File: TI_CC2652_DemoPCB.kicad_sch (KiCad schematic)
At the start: 4 parts

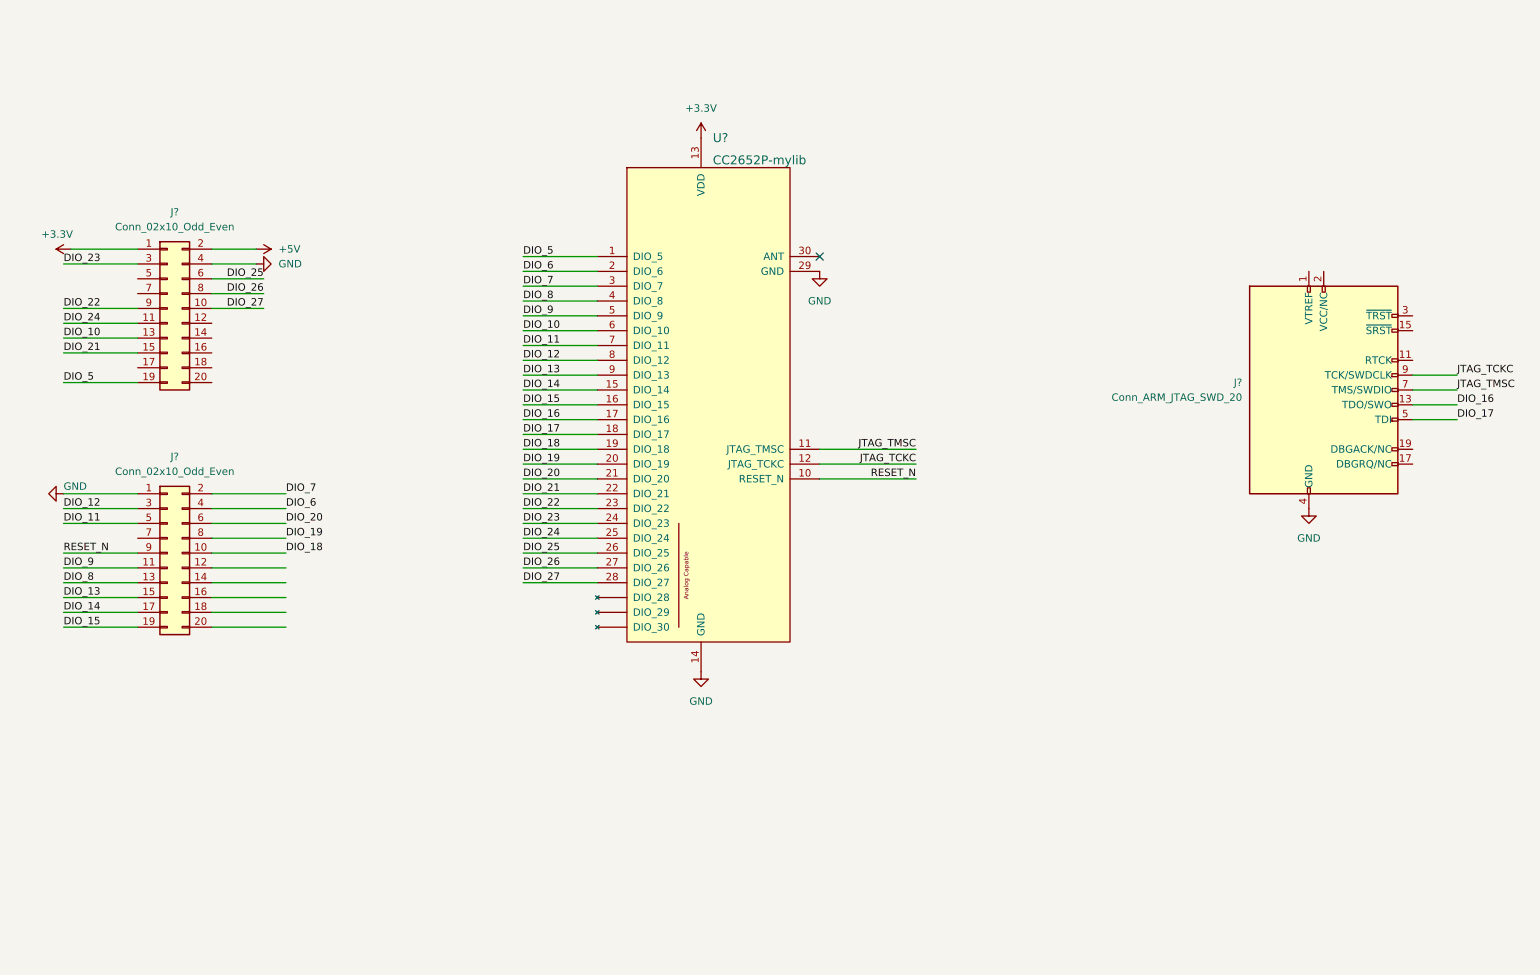
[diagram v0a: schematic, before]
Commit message: LEDs Added
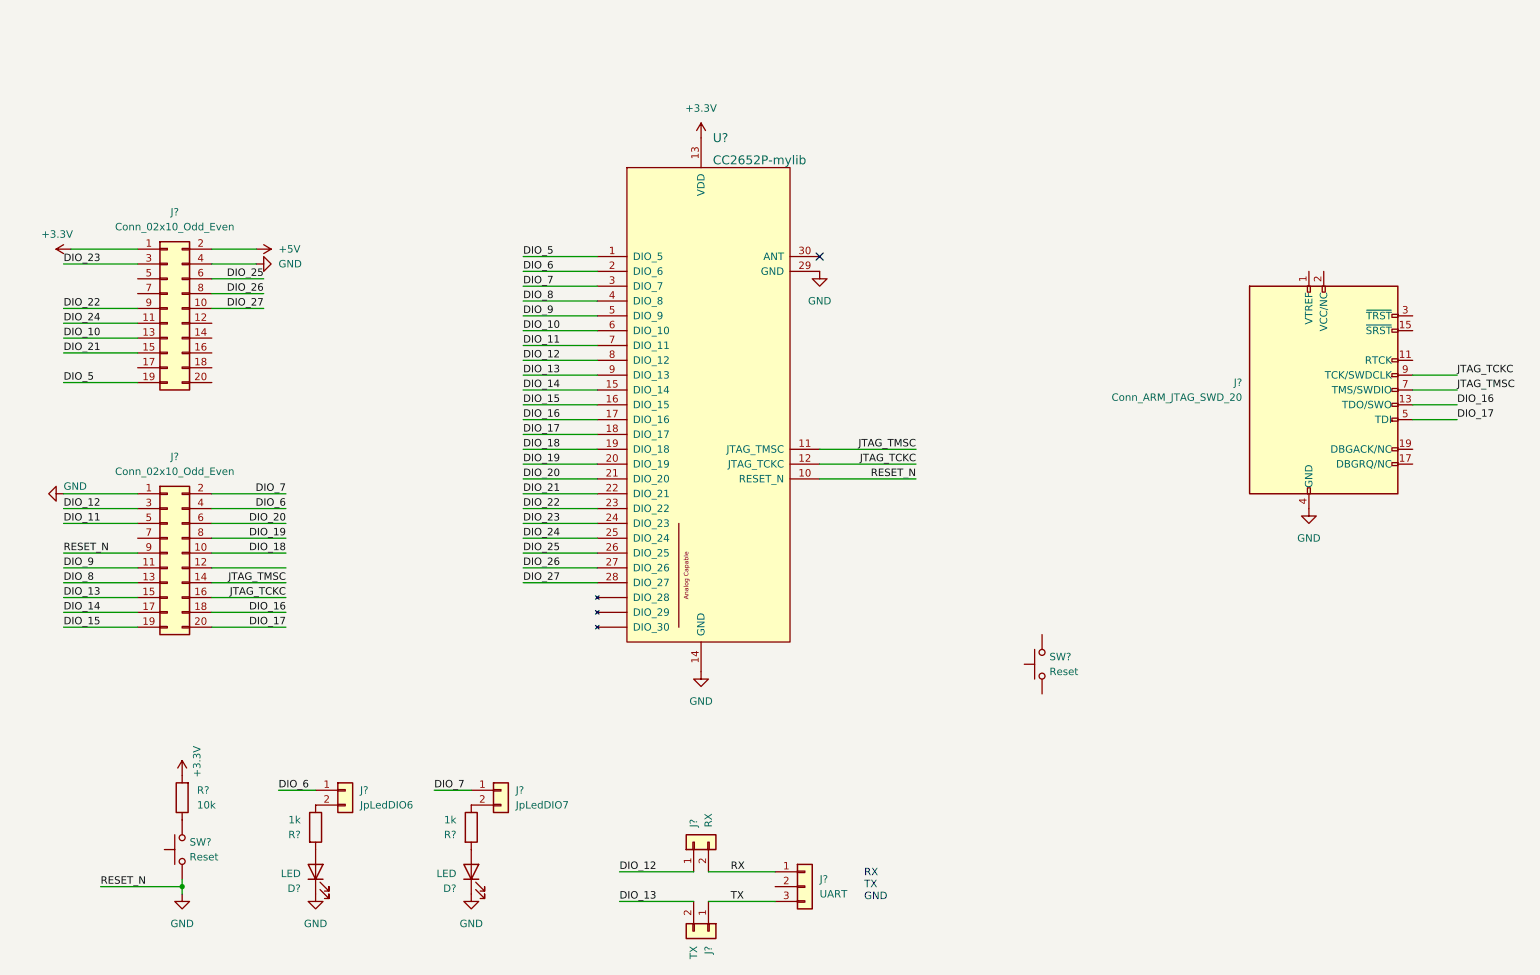
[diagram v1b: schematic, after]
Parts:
- added D? (x2): LED, symbol Device:LED
- added J?: JpLedDIO6, symbol Connector_Generic:Conn_01x02
- added J?: UART, symbol Connector_Generic:Conn_01x03
- added J?: JpLedDIO7, symbol Connector_Generic:Conn_01x02
- added J?: TX, symbol Connector_Generic:Conn_01x02
- added J?: RX, symbol Connector_Generic:Conn_01x02
- added R? (x2): 1k, Resistor_SMD:R_1206_3216Metric, symbol Device:R
- added R?: 10k, Resistor_SMD:R_1206_3216Metric, symbol Device:R
- added SW? (x2): Reset, symbol Switch:SW_Push
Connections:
- net RESET_N is gone; now on net GND: J?.9 (Pin_9), U?.10 (RESET_N)
- net +3V3: now also R?.2
- net DIO_12: now also J?.1 (Pin_1)
- net DIO_13: now also J?.2 (Pin_2)
- net DIO_16: now also J?.18 (Pin_18)
- net DIO_17: now also J?.20 (Pin_20)
- net DIO_6: now also J?.1 (Pin_1)
- net DIO_7: now also J?.1 (Pin_1)
- net GND: now also D?.1 (K), D?.1 (K), SW?.1
- net JTAG_TCKC: now also J?.16 (Pin_16)
- net JTAG_TMSC: now also J?.14 (Pin_14)
- new net: J?.2 (Pin_2), R?.1 (x2)
- new net: D?.2 (A), R?.2 (x2)
- new net: R?.1, SW?.2
- new net RX: J?.1 (Pin_1), J?.2 (Pin_2)
- new net TX: J?.1 (Pin_1), J?.3 (Pin_3)
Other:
- note added: "RX TX GND"

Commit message: PCB added
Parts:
- added C1: 0.1, Capacitor_SMD:C_0805_2012Metric, symbol Device:C
- added D3: LED, LED_SMD:LED_0805_2012Metric, symbol Device:LED
- added J8: Conn_01x02, myTerminal:DG142V-5.08-2, symbol Connector_Generic:Conn_01x02
- added R4: 1k, Resistor_SMD:R_1206_3216Metric, symbol Device:R
- added SW2: BSL, Button_Switch_THT:SW_PUSH_6mm_H4.3mm, symbol Switch:SW_Push
- added U2: LM2596Module, myPowerManagement:LM2596Module, symbol myPowerManagement:LM2596Module
- D1, D2: renamed from D?; footprint (none) -> LED_SMD:LED_0805_2012Metric
- J1, J2: renamed from J?; footprint (none) -> Connector_PinHeader_2.54mm:PinHeader_2x10_P2.54mm_Vertical
- J3, J4, J5, J6: renamed from J?; footprint (none) -> Connector_PinHeader_2.54mm:PinHeader_1x02_P2.54mm_Vertical
- J7: renamed from J?; footprint (none) -> Connector_PinHeader_2.54mm:PinHeader_1x03_P2.54mm_Vertical
- SW1: renamed from SW?; footprint (none) -> Button_Switch_THT:SW_PUSH_6mm_H4.3mm
- SW3: renamed from SW?; value Reset -> BSL; footprint (none) -> Button_Switch_THT:SW_PUSH_6mm_H4.3mm
- U1: renamed from U?; footprint myLib:RF-BM-2652P2 -> myZigbee:RF-BM-2652P2
- gave numbers to parts that had none: 4
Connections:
- net +5V is gone; now on net +3V3: J1.2 (Pin_2)
- net +3V3: now also J1.4 (Pin_4), J1.6 (Pin_6), J2.16 (Pin_16), J2.18 (Pin_18), J2.20 (Pin_20), R4.1, U2.4 (+); no longer J1.1 (Pin_1)
- net DIO_10: now also J1.11 (Pin_11); no longer J1.13 (Pin_13)
- net DIO_11: now also J1.13 (Pin_13); no longer J2.5 (Pin_5)
- net DIO_12: now also J1.15 (Pin_15); no longer J2.3 (Pin_3)
- net DIO_13: now also J1.17 (Pin_17); no longer J2.15 (Pin_15)
- net DIO_14: now also J2.8 (Pin_8), SW2.1; no longer J2.17 (Pin_17)
- net DIO_15: now also J2.6 (Pin_6), SW3.1; no longer J2.19 (Pin_19)
- net DIO_16: now also J2.4 (Pin_4); no longer J2.18 (Pin_18)
- net DIO_17: now also J2.2 (Pin_2); no longer J2.20 (Pin_20)
- net DIO_18: now also J2.1 (Pin_1); no longer J2.10 (Pin_10)
- net DIO_19: now also J2.3 (Pin_3); no longer J2.8 (Pin_8)
- net DIO_20: now also J2.5 (Pin_5); no longer J2.6 (Pin_6)
- net DIO_21: now also J2.7 (Pin_7); no longer J1.15 (Pin_15)
- net DIO_22: now also J2.9 (Pin_9); no longer J1.9 (Pin_9)
- net DIO_23: now also J2.11 (Pin_11); no longer J1.3 (Pin_3)
- net DIO_24: now also J2.13 (Pin_13); no longer J1.11 (Pin_11)
- net DIO_25: now also J2.15 (Pin_15); no longer J1.6 (Pin_6)
- net DIO_26: now also J2.17 (Pin_17); no longer J1.8 (Pin_8)
- net DIO_27: now also J2.19 (Pin_19); no longer J1.10 (Pin_10)
- net DIO_5: now also J1.1 (Pin_1); no longer J1.19 (Pin_19)
- net DIO_6: now also J1.3 (Pin_3); no longer J2.4 (Pin_4)
- net DIO_7: now also J1.5 (Pin_5); no longer J2.2 (Pin_2)
- net DIO_8: now also J1.7 (Pin_7); no longer J2.13 (Pin_13)
- net DIO_9: now also J1.9 (Pin_9); no longer J2.11 (Pin_11)
- net GND: now also J1.10 (Pin_10), J1.12 (Pin_12), J1.14 (Pin_14), J1.16 (Pin_16), J1.8 (Pin_8), J2.10 (Pin_10), J2.12 (Pin_12), J2.14 (Pin_14), J7.3 (Pin_3), SW3.2, C1.2, D3.1 (K), SW2.2, U2.3 (-); no longer J1.4 (Pin_4), J2.1 (Pin_1), J2.9 (Pin_9), U1.10 (RESET_N)
- net JTAG_TCKC: now also J1.18 (Pin_18); no longer J2.16 (Pin_16)
- net JTAG_TMSC: now also J1.20 (Pin_20); no longer J2.14 (Pin_14)
- net TX: now also J7.2 (Pin_2); no longer J7.3 (Pin_3)
- net RESET_N: now reaches R1.1, SW1.2
- net RESET_N: now also J1.19 (Pin_19), U1.10 (RESET_N), C1.1
- new net: D3.2 (A), R4.2
- new net +24V: J8.2 (Pin_2), U2.1 (+)
- new net GNDPWR: J8.1 (Pin_1), U2.2 (-)
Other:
- moved on the sheet: R1, SW1, SW3

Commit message: сс2652 module moved to top side
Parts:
- added J10: JpSWDIO14, Connector_PinHeader_2.54mm:PinHeader_1x02_P2.54mm_Vertical, symbol Connector_Generic:Conn_01x02
- added J11: JpSWDIO15, Connector_PinHeader_2.54mm:PinHeader_1x02_P2.54mm_Vertical, symbol Connector_Generic:Conn_01x02
- SW2: value BSL -> SW2
- SW3: value BSL -> SW3
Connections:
- net +3V3: now also J1.1 (Pin_1), J1.3 (Pin_3), J1.5 (Pin_5), J2.15 (Pin_15), J2.17 (Pin_17), J2.19 (Pin_19); no longer J1.2 (Pin_2), J1.4 (Pin_4), J1.6 (Pin_6), J2.16 (Pin_16), J2.18 (Pin_18), J2.20 (Pin_20)
- net DIO_10: now also J1.12 (Pin_12); no longer J1.11 (Pin_11)
- net DIO_11: now also J1.14 (Pin_14); no longer J1.13 (Pin_13)
- net DIO_12: now also J1.16 (Pin_16); no longer J1.15 (Pin_15)
- net DIO_13: now also J1.18 (Pin_18), J6.1 (Pin_1); no longer J1.17 (Pin_17), J6.2 (Pin_2)
- net DIO_14: now also J2.7 (Pin_7), J10.1 (Pin_1); no longer J2.8 (Pin_8), SW2.1
- net DIO_15: now also J2.5 (Pin_5), J11.1 (Pin_1); no longer J2.6 (Pin_6), SW3.1
- net DIO_16: now also J2.3 (Pin_3); no longer J2.4 (Pin_4)
- net DIO_17: now also J2.1 (Pin_1); no longer J2.2 (Pin_2)
- net DIO_18: now also J2.2 (Pin_2); no longer J2.1 (Pin_1)
- net DIO_19: now also J2.4 (Pin_4); no longer J2.3 (Pin_3)
- net DIO_20: now also J2.6 (Pin_6); no longer J2.5 (Pin_5)
- net DIO_21: now also J2.8 (Pin_8); no longer J2.7 (Pin_7)
- net DIO_22: now also J2.10 (Pin_10); no longer J2.9 (Pin_9)
- net DIO_23: now also J2.12 (Pin_12); no longer J2.11 (Pin_11)
- net DIO_24: now also J2.14 (Pin_14); no longer J2.13 (Pin_13)
- net DIO_25: now also J2.16 (Pin_16); no longer J2.15 (Pin_15)
- net DIO_26: now also J2.18 (Pin_18); no longer J2.17 (Pin_17)
- net DIO_27: now also J2.20 (Pin_20); no longer J2.19 (Pin_19)
- net DIO_5: now also J1.2 (Pin_2); no longer J1.1 (Pin_1)
- net DIO_6: now also J1.4 (Pin_4); no longer J1.3 (Pin_3)
- net DIO_7: now also J1.6 (Pin_6); no longer J1.5 (Pin_5)
- net DIO_8: now also J1.8 (Pin_8); no longer J1.7 (Pin_7)
- net DIO_9: now also J1.10 (Pin_10); no longer J1.9 (Pin_9)
- net GND: now also J1.11 (Pin_11), J1.13 (Pin_13), J1.15 (Pin_15), J1.7 (Pin_7), J1.9 (Pin_9), J2.11 (Pin_11), J2.13 (Pin_13), J2.9 (Pin_9); no longer J1.10 (Pin_10), J1.12 (Pin_12), J1.14 (Pin_14), J1.16 (Pin_16), J1.8 (Pin_8), J2.10 (Pin_10), J2.12 (Pin_12), J2.14 (Pin_14)
- net JTAG_TCKC: now also J1.17 (Pin_17); no longer J1.18 (Pin_18)
- net JTAG_TMSC: now also J1.19 (Pin_19); no longer J1.20 (Pin_20)
- net RESET_N: now also J1.20 (Pin_20); no longer J1.19 (Pin_19)
- net TX: now also J6.2 (Pin_2); no longer J6.1 (Pin_1)
- new net: J11.2 (Pin_2), SW3.1
- new net: J10.2 (Pin_2), SW2.1
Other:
- moved on the sheet: J6, SW2, SW3
